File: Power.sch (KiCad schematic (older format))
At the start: 4 parts, among them J5 XT30, U12 U74AHC1G04G-AL5-R, U13 74LVC1G08GV, U14 NC7SZ02M5X

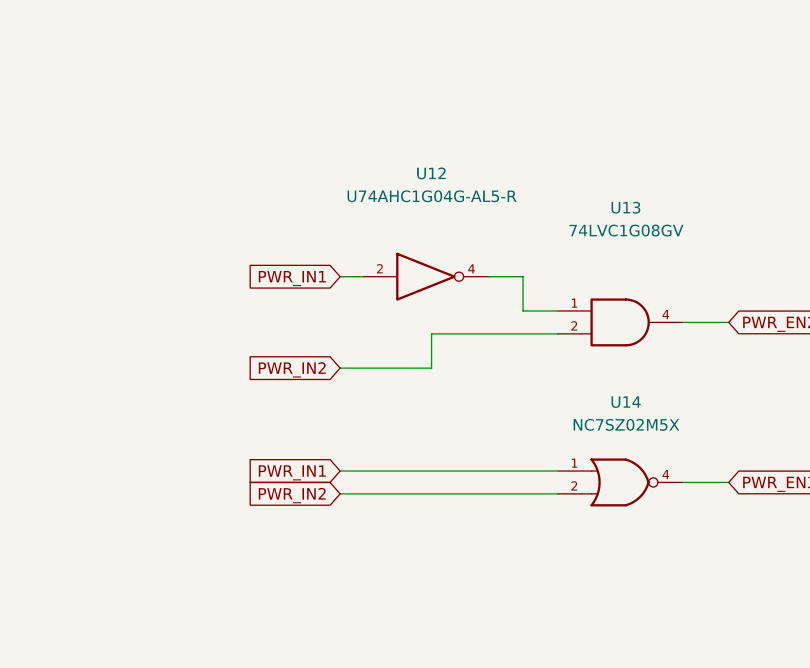
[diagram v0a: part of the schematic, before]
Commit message: start adding usb-c
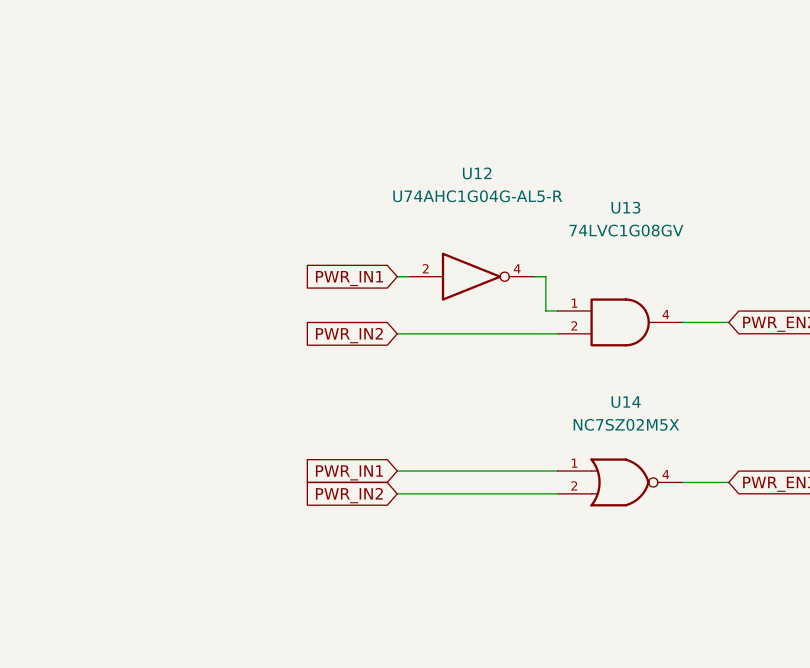
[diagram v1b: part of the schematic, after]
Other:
- moved on the sheet: U12
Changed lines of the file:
@@
 L 74xGxx:74AHC1G04 U12
 U 1 1 61C53331
-P 2500 2300
-F 0 "U12" H 2500 2750 50  0000 C CNN
-F 1 "U74AHC1G04G-AL5-R" H 2500 2650 50  0000 C CNN
-F 2 "Package_TO_SOT_SMD:SOT-353_SC-70-5" H 2500 2300 50  0001 C CNN
-F 3 "http://www.ti.com/lit/sg/scyt129e/scyt129e.pdf" H 2500 2300 50  0001 C CNN
-F 4 "U74AHC1G04G-AL5-R" H 2500 2300 50  0001 C CNN "Manufacturer_Part_Number"
-F 5 "http://www.ti.com/lit/sg/scyt129e/scyt129e.pdf" H 2500 2300 50  0001 C CNN "Datasheet"
-F 6 "Package_TO_SOT_SMD:SOT-353_SC-70-5" H 2500 2300 50  0001 C CNN "Footprint"
-F 7 "U12" H 2500 2300 50  0001 C CNN "Reference"
-F 8 "U74AHC1G04G-AL5-R" H 2500 2300 50  0001 C CNN "Value"
-	1    2500 2300
+P 2700 2300
+F 0 "U12" H 2700 2750 50  0000 C CNN
+F 1 "U74AHC1G04G-AL5-R" H 2700 2650 50  0000 C CNN
+F 2 "Package_TO_SOT_SMD:SOT-353_SC-70-5" H 2700 2300 50  0001 C CNN
+F 3 "http://www.ti.com/lit/sg/scyt129e/scyt129e.pdf" H 2700 2300 50  0001 C CNN
+F 4 "U74AHC1G04G-AL5-R" H 2700 2300 50  0001 C CNN "Manufacturer_Part_Number"
+F 5 "http://www.ti.com/lit/sg/scyt129e/scyt129e.pdf" H 2700 2300 50  0001 C CNN "Datasheet"
+F 6 "Package_TO_SOT_SMD:SOT-353_SC-70-5" H 2700 2300 50  0001 C CNN "Footprint"
+F 7 "U12" H 2700 2300 50  0001 C CNN "Reference"
+F 8 "U74AHC1G04G-AL5-R" H 2700 2300 50  0001 C CNN "Value"
+	1    2700 2300
 	1    0    0    -1
 $EndComp
@@
 	1    0    0    -1
 $EndComp
-Text GLabel 2100 2300 0    50   Input ~ 0
+Text GLabel 2350 2300 0    50   Input ~ 0
 PWR_IN1
-Text GLabel 2100 3150 0    50   Input ~ 0
+Text GLabel 2350 3150 0    50   Input ~ 0
 PWR_IN1
-Text GLabel 2100 2700 0    50   Input ~ 0
+Text GLabel 2350 2550 0    50   Input ~ 0
 PWR_IN2
 Text GLabel 3800 2500 2    50   Input ~ 0
@@
 Text GLabel 3800 3200 2    50   Input ~ 0
 PWR_EN3
-Text GLabel 2100 3250 0    50   Input ~ 0
+Text GLabel 2350 3250 0    50   Input ~ 0
 PWR_IN2
 Wire Wire Line
-	2100 2700 2500 2700
+	2350 2550 3050 2550
 Wire Wire Line
-	2500 2700 2500 2550
+	2950 2300 3000 2300
 Wire Wire Line
-	2500 2550 3050 2550
+	3000 2300 3000 2450
 Wire Wire Line
-	2750 2300 2900 2300
-Wire Wire Line
-	2900 2300 2900 2450
-Wire Wire Line
-	2900 2450 3050 2450
+	3000 2450 3050 2450
 Wire Wire Line
 	3600 2500 3800 2500
 Wire Wire Line
-	2200 2300 2100 2300
+	2400 2300 2350 2300
 Wire Wire Line
-	3050 3150 2100 3150
+	3050 3150 2350 3150
 Wire Wire Line
-	2100 3250 3050 3250
+	2350 3250 3050 3250
 Wire Wire Line
 	3600 3200 3800 3200

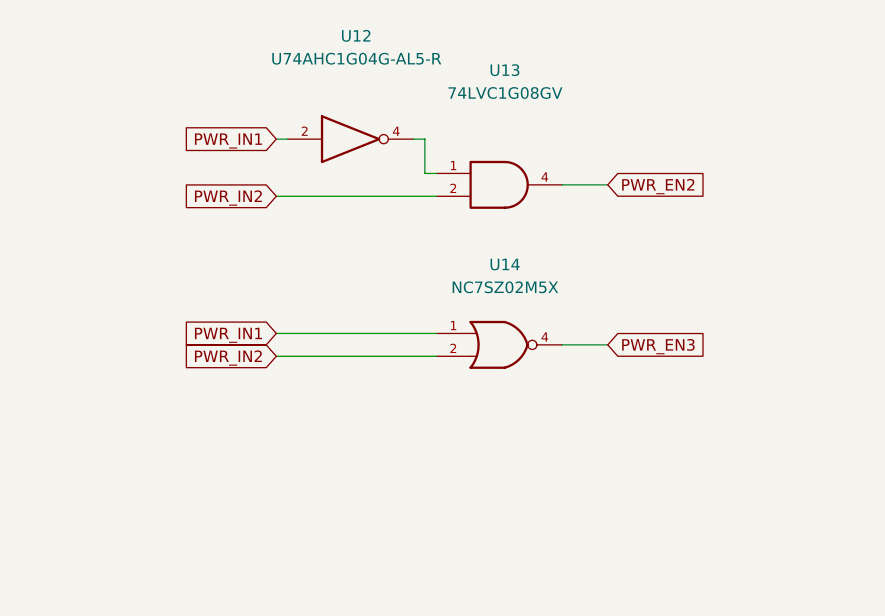
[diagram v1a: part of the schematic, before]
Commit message: start migrating to kicad v6
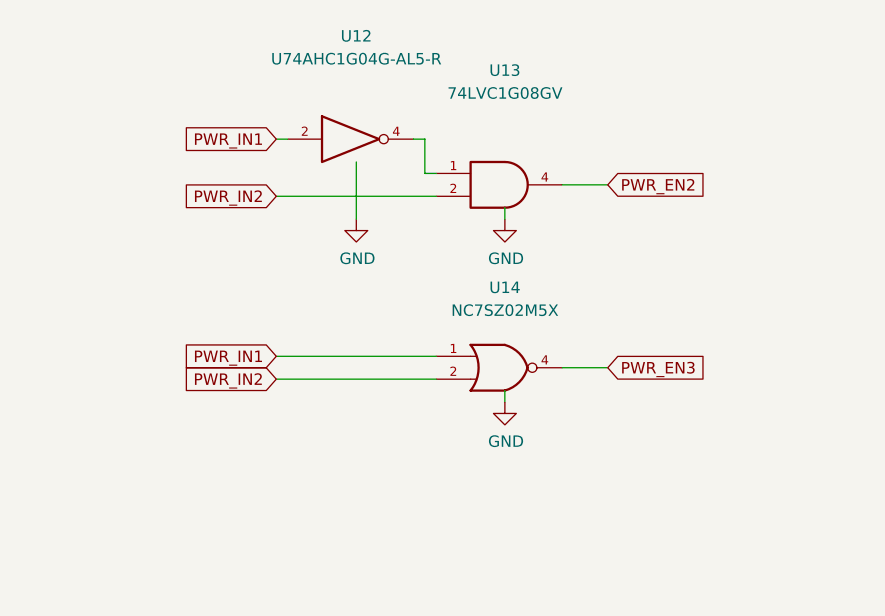
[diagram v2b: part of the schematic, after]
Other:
- moved on the sheet: U14
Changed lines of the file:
@@
 L 74xGxx:74AHC1G02 U14
 U 1 1 61CD2B59
-P 3350 3200
-F 0 "U14" H 3350 3550 50  0000 C CNN
-F 1 "NC7SZ02M5X" H 3350 3450 50  0000 C CNN
-F 2 "Package_TO_SOT_SMD:SOT-23-5" H 3350 3200 50  0001 C CNN
-F 3 "http://www.ti.com/lit/sg/scyt129e/scyt129e.pdf" H 3350 3200 50  0001 C CNN
-F 4 "NC7SZ02M5X" H 3350 3200 50  0001 C CNN "Manufacturer_Part_Number"
-F 5 "http://www.ti.com/lit/sg/scyt129e/scyt129e.pdf" H 3350 3200 50  0001 C CNN "Datasheet"
-F 6 "Package_TO_SOT_SMD:SOT-23-5" H 3350 3200 50  0001 C CNN "Footprint"
-F 7 "U14" H 3350 3200 50  0001 C CNN "Reference"
-F 8 "NC7SZ02M5X" H 3350 3200 50  0001 C CNN "Value"
-	1    3350 3200
+P 3350 3300
+F 0 "U14" H 3350 3650 50  0000 C CNN
+F 1 "NC7SZ02M5X" H 3350 3550 50  0000 C CNN
+F 2 "Package_TO_SOT_SMD:SOT-23-5" H 3350 3300 50  0001 C CNN
+F 3 "http://www.ti.com/lit/sg/scyt129e/scyt129e.pdf" H 3350 3300 50  0001 C CNN
+F 4 "NC7SZ02M5X" H 3350 3300 50  0001 C CNN "Manufacturer_Part_Number"
+F 5 "http://www.ti.com/lit/sg/scyt129e/scyt129e.pdf" H 3350 3300 50  0001 C CNN "Datasheet"
+F 6 "Package_TO_SOT_SMD:SOT-23-5" H 3350 3300 50  0001 C CNN "Footprint"
+F 7 "U14" H 3350 3300 50  0001 C CNN "Reference"
+F 8 "NC7SZ02M5X" H 3350 3300 50  0001 C CNN "Value"
+	1    3350 3300
 	1    0    0    -1
 $EndComp
 Text GLabel 2350 2300 0    50   Input ~ 0
 PWR_IN1
-Text GLabel 2350 3150 0    50   Input ~ 0
+Text GLabel 2350 3250 0    50   Input ~ 0
 PWR_IN1
 Text GLabel 2350 2550 0    50   Input ~ 0
@@
 Text GLabel 3800 2500 2    50   Input ~ 0
 PWR_EN2
-Text GLabel 3800 3200 2    50   Input ~ 0
+Text GLabel 3800 3300 2    50   Input ~ 0
 PWR_EN3
-Text GLabel 2350 3250 0    50   Input ~ 0
+Text GLabel 2350 3350 0    50   Input ~ 0
 PWR_IN2
 Wire Wire Line
@@
 	2400 2300 2350 2300
 Wire Wire Line
-	3050 3150 2350 3150
+	3050 3250 2350 3250
 Wire Wire Line
-	2350 3250 3050 3250
+	2350 3350 3050 3350
 Wire Wire Line
-	3600 3200 3800 3200
+	3600 3300 3800 3300
+$Comp
+L power:GND #PWR08
+U 1 1 61CE2503
+P 3350 2650
+F 0 "#PWR08" H 3350 2400 50  0001 C CNN
+F 1 "GND" H 3355 2477 50  0000 C CNN
+F 2 "" H 3350 2650 50  0001 C CNN
+F 3 "" H 3350 2650 50  0001 C CNN
+	1    3350 2650
+	1    0    0    -1
+$EndComp
+$Comp
+L power:GND #PWR09
+U 1 1 61CE2903
+P 3350 3450
+F 0 "#PWR09" H 3350 3200 50  0001 C CNN
+F 1 "GND" H 3355 3277 50  0000 C CNN
+F 2 "" H 3350 3450 50  0001 C CNN
+F 3 "" H 3350 3450 50  0001 C CNN
+	1    3350 3450
+	1    0    0    -1
+$EndComp
+$Comp
+L power:GND #PWR07
+U 1 1 61CE462E
+P 2700 2650
+F 0 "#PWR07" H 2700 2400 50  0001 C CNN
+F 1 "GND" H 2705 2477 50  0000 C CNN
+F 2 "" H 2700 2650 50  0001 C CNN
+F 3 "" H 2700 2650 50  0001 C CNN
+	1    2700 2650
+	1    0    0    -1
+$EndComp
+Wire Wire Line
+	3350 3450 3350 3400
+Wire Wire Line
+	3350 2650 3350 2600
+Wire Wire Line
+	2700 2400 2700 2650
 $EndSCHEMATC
